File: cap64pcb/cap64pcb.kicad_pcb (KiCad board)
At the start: 2 copper layers, 91.6 x 12 mm, 31 parts, among them J1 SM05B_SURS_TF, Q1 BSS138, Q2 BSS138, U1 MPR121QR2, U2 SPX3819M5-L-3-3

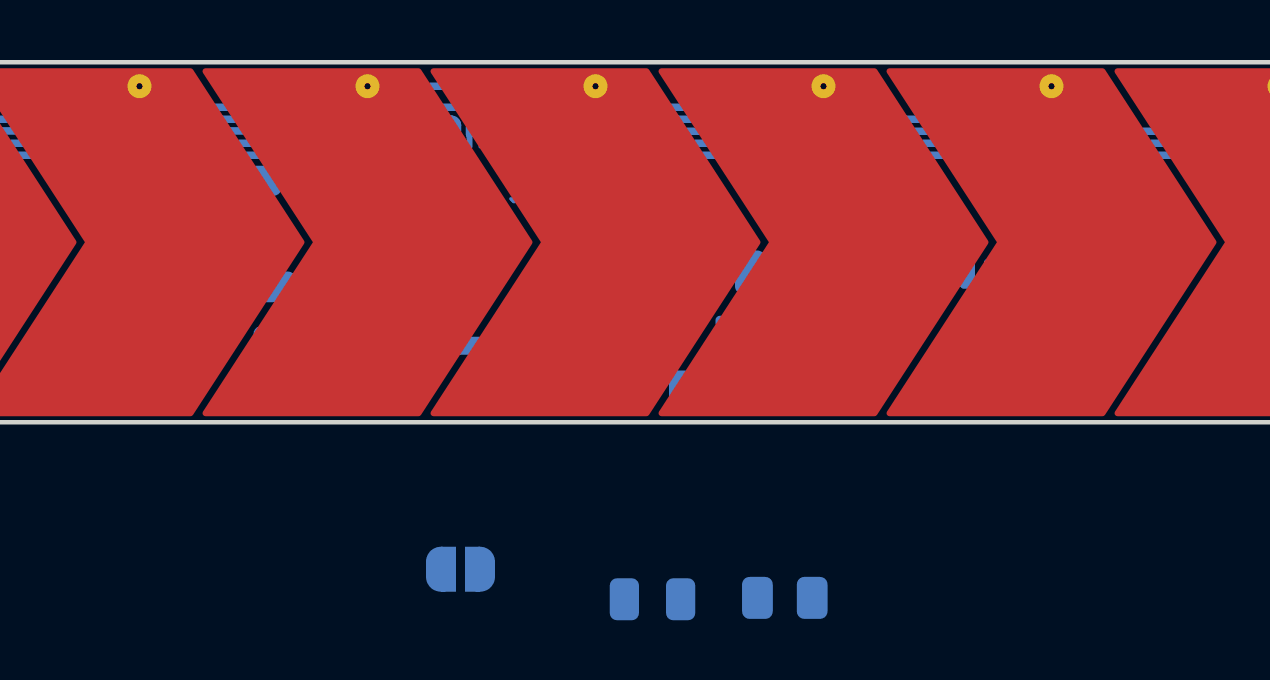
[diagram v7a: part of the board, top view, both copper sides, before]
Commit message: tie MP to GND
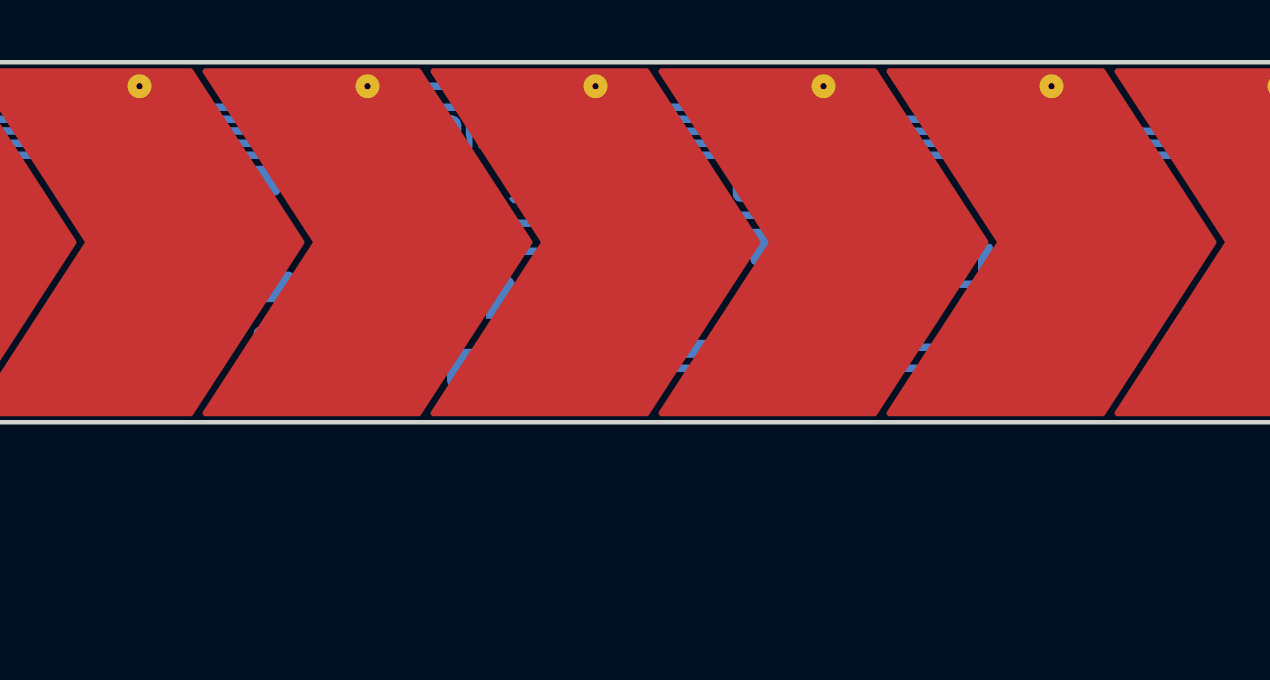
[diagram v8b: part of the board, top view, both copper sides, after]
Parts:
- moved R4 13.0 mm to (85.1, 44.9), turned to -90 degrees
- moved D1 11.9 mm to (83.1, 45.3), turned to -90 degrees
- moved JP2 9.31 mm to (80.0, 46.8), turned to 180 degrees
- moved C2 6.76 mm to (89.1, 44.1), turned to -90 degrees
- moved JP3 6.64 mm to (80.0, 49.3)
- moved U2 4.94 mm to (91.8, 44.3), turned to 90 degrees
- moved Q1 4.08 mm to (84.2, 48.7)
- moved R2 3.98 mm to (87.1, 44.1)
- moved Q2 2.90 mm to (88.1, 47.6)
- moved C1 2.40 mm to (91.8, 47.4)
- moved J1 1.49 mm to (97.2, 44.4)
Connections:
- J1 pad 1: VCC -> GND
- J1 pad 2: Net-(J1-Pad2) -> VCC
- J1 pad 4: GND -> Net-(J1-Pad4)
- Q1 pad 3: Net-(J1-Pad2) -> Net-(J1-Pad3)
- Q2 pad 3: Net-(J1-Pad3) -> Net-(J1-Pad4)
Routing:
- net Net-(J1-Pad3): track 0.00 -> 20.8 mm
- net +3V3: track 0.00 -> 14.8 mm
- net Net-(J1-Pad4): track 0.00 -> 12.7 mm
- net GND: track 0.00 -> 11.6 mm
- net SCL: track 0.00 -> 9.69 mm
- net VCC: track 0.00 -> 9.57 mm
- net Net-(U1-Pad1): track 0.00 -> 2.37 mm
- net Net-(D1-Pad2): track 0.00 -> 2.18 mm
- net Net-(R1-Pad1): track 0.00 -> 2.14 mm
- net Net-(C2-Pad1): track 0.00 -> 1.81 mm
